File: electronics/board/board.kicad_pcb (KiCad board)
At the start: 2 copper layers, 58 parts, among them J1 Screw_Terminal_01x02, J10 Conn_01x02, J11 Conn_01x02, J12 Conn_01x02, J13 Conn_01x02, J14 Conn_01x02, J15 Conn_01x02, J16 Conn_01x02, J17 Conn_01x02, J18 Conn_01x02, J19 Conn_01x02, J2 Screw_Terminal_01x02, J20 Conn_01x02, J21 Conn_01x02, J22 Conn_01x02, J23 Screw_Terminal_01x01, J25 Screw_Terminal_01x01, J3 AVR-ISP-6, J4 USB_B_Micro, J5 Screw_Terminal_01x02, J6 Screw_Terminal_01x02, J7 Conn_01x02, J8 Conn_01x02, J9 Conn_01x02, Q1 IRF7404, SW1 SW_Push_Open_Dual, U1 LMV358, U2 ATmega32U4-AU, U3 LM7805_TO220, U4 ST485EBDR, U5 ULN2803A, U6 ULN2803A, Y1 Crystal 16MHz

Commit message: Footprint placement v1
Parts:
- moved J5 152.0 mm to (182.9, 147.3), turned to 180 degrees
- moved D3 143.0 mm to (202.9, 163.8)
- moved D2 142.6 mm to (174.0, 147.2)
- moved C7 136.8 mm to (181.1, 161.3), turned to 0 degrees
- moved R3 136.7 mm to (187.5, 161.3)
- moved R7 136.4 mm to (198.6, 163.8)
- moved U3 132.9 mm to (168.9, 146.1), turned to 180 degrees
- moved D1 130.3 mm to (189.7, 153.7)
- moved SW1 129.4 mm to (191.1, 146.7)
- moved U4 126.4 mm to (156.4, 147.3), turned to 180 degrees
- moved R8 122.9 mm to (159.5, 152.4), turned to 0 degrees
- moved J6 112.7 mm to (199.4, 148.6)
- moved J1 101.8 mm to (71.1, 146.1)
- moved J2 94.5 mm to (69.8, 160.0)
- moved J4 90.1 mm to (203.3, 157.1)
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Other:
- board outline added: 141 x 30.5 mm

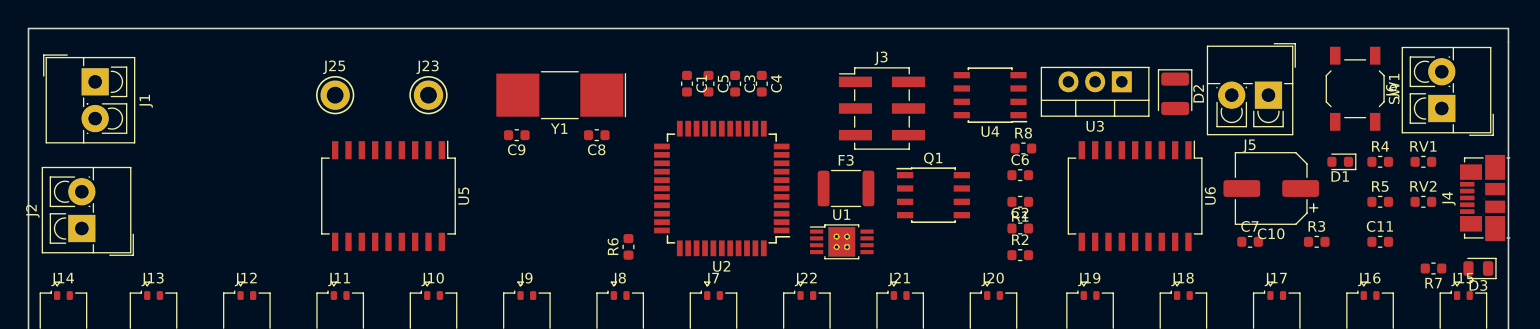
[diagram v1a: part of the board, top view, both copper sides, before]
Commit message: 5V regulator bug
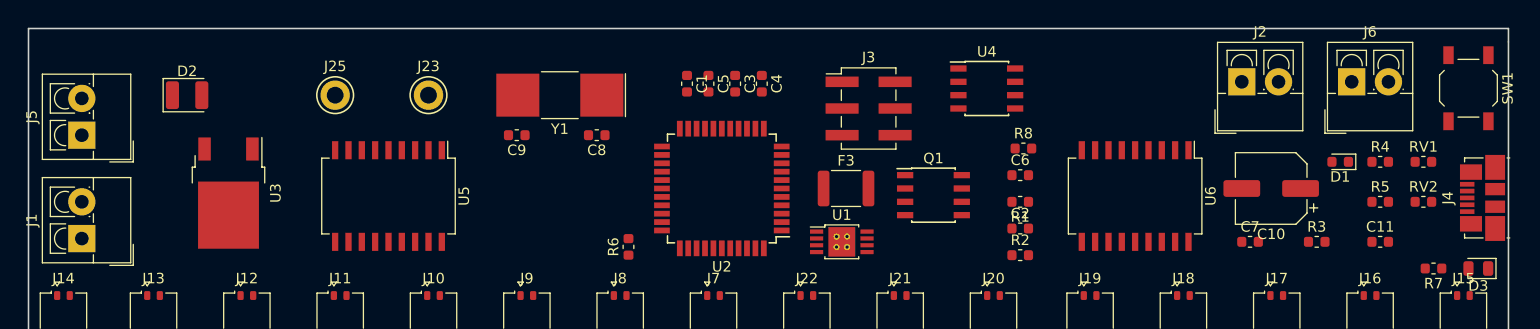
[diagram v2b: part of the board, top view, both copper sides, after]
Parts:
- U3: value LM7805_TO220 -> NCP1117-5.0_TO252; footprint Package_TO_SOT_THT:TO-220-3_Vertical -> Package_TO_SOT_SMD:TO-252-2
- moved J5 113.1 mm to (69.8, 151.1), turned to 90 degrees
- moved J2 111.4 mm to (180.3, 146.1), turned to 0 degrees
- moved D2 94.1 mm to (79.9, 147.3), turned to 0 degrees
- moved U3 85.7 mm to (83.8, 156.7), turned to 270 degrees
- moved J1 15.0 mm to (69.8, 161.0), turned to 90 degrees
- moved SW1 10.8 mm to (201.9, 146.7)
- moved J6 8.95 mm to (190.8, 146.1), turned to 0 degrees
- moved J3 1.27 mm to (144.8, 148.6)
- moved U4 0.71 mm to (156.1, 146.7), turned to 0 degrees
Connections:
- U3 pad 1: +12V -> GND
- U3 pad 2: GND -> +5V
- U3 pad 3: +5V -> +12V

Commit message: Routing update
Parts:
- moved C9 25.6 mm to (136.4, 146.1)
- moved C1 22.6 mm to (110.8, 161.4)
- moved C5 21.5 mm to (114.3, 161.4)
- moved C3 20.8 mm to (117.9, 161.4)
- moved C4 20.1 mm to (121.5, 161.4)
- moved J25 14.7 mm to (108.5, 144.5)
- moved C8 13.6 mm to (131.5, 146.1)
- moved J23 10.3 mm to (112.8, 144.5)
- moved R6 7.64 mm to (121.4, 154.2), turned to 270 degrees
- moved R1 7.46 mm to (153.2, 161.8), turned to 270 degrees
- moved Y1 6.43 mm to (121.5, 145.3), turned to 0 degrees
- moved R5 5.43 mm to (192.5, 162.8)
- moved C11 2.50 mm to (192.5, 159.0)
- moved Q1 1.89 mm to (152.6, 155.8)
- moved R7 1.79 mm to (197.1, 162.8)
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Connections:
- J1 pad 1: +12V -> Net-(D2-Pad1)
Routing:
- net +5V: track 0.00 -> 226.6 mm, vias 0 -> 3
- net /RESET: track 0.00 -> 95.4 mm, vias 0 -> 3
- net +12V: track 0.00 -> 92.4 mm, vias 0 -> 2
- net Net-(J10-Pad2): track 0.00 -> 80.8 mm, vias 0 -> 2
- net Net-(J15-Pad2): track 0.00 -> 80.6 mm, vias 0 -> 2
- net Net-(F3-Pad2): track 0.00 -> 67.8 mm, vias 0 -> 2
- net VBUS: track 0.00 -> 66.5 mm, vias 0 -> 3
- net Net-(R4-Pad1): track 0.00 -> 65.5 mm, vias 0 -> 4
- net Net-(R5-Pad1): track 0.00 -> 57.4 mm, vias 0 -> 2
- net Net-(U2-Pad26): track 0.00 -> 54.3 mm, vias 0 -> 2
- net Net-(U2-Pad27): track 0.00 -> 52.0 mm, vias 0 -> 2
- net Net-(U2-Pad41): track 0.00 -> 45.2 mm, vias 0 -> 2
- net Net-(U2-Pad40): track 0.00 -> 44.9 mm, vias 0 -> 2
- net Net-(U2-Pad39): track 0.00 -> 44.5 mm, vias 0 -> 2
- net Net-(U2-Pad37): track 0.00 -> 44.4 mm, vias 0 -> 2
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
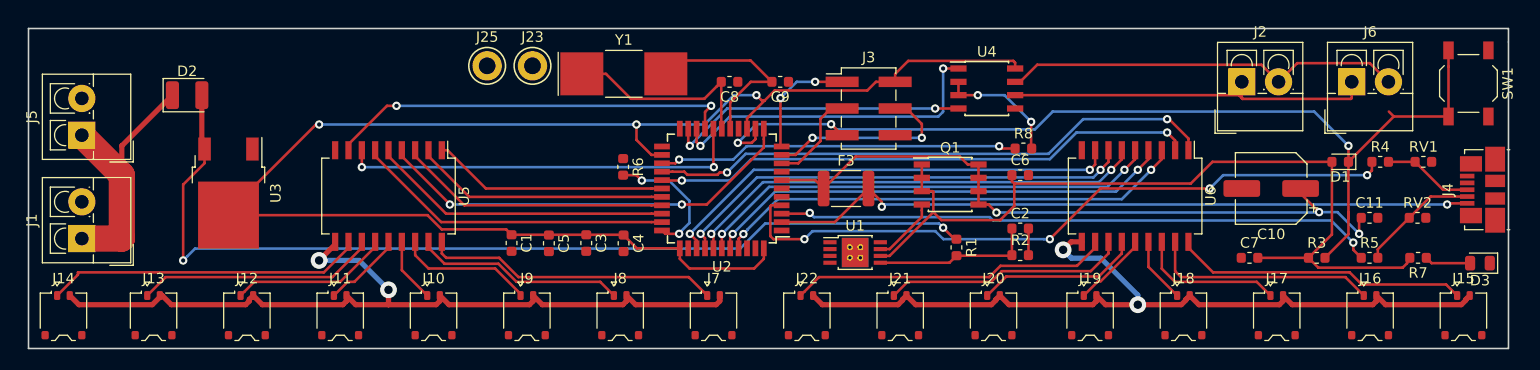
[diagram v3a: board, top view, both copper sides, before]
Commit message: GND + mounting holes
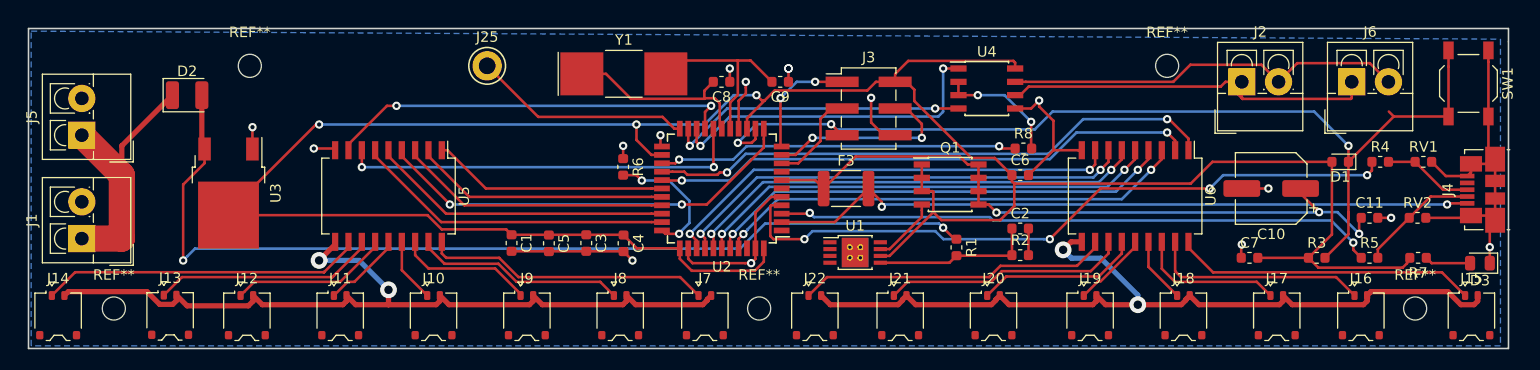
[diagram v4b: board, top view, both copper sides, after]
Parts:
- removed J23: Screw_Terminal_01x01, TestPoint:TestPoint_Keystone_5005-5009_Compact
- added REF**: MountingHole_2.2mm_M2, MountingHole:MountingHole_2.2mm_M2, F.Cu at (134.4, 167.6)
- added REF**: MountingHole_2.2mm_M2, MountingHole:MountingHole_2.2mm_M2, F.Cu at (196.8, 167.6)
- added REF**: MountingHole_2.2mm_M2, MountingHole:MountingHole_2.2mm_M2, F.Cu at (72.9, 167.6)
- added REF**: MountingHole_2.2mm_M2, MountingHole:MountingHole_2.2mm_M2, F.Cu at (173.2, 144.5)
- added REF**: MountingHole_2.2mm_M2, MountingHole:MountingHole_2.2mm_M2, F.Cu at (85.9, 144.5)
- moved J13 1.58 mm to (78.3, 168.2)
- moved J16 0.88 mm to (191.7, 168.3)
- moved J7 0.83 mm to (129.2, 168.3)
- moved C8 0.76 mm to (130.8, 146.1)
- moved J15 0.76 mm to (202.2, 168.3)
- moved J22 0.76 mm to (139.7, 168.3)
- moved J14 0.51 mm to (67.6, 168.3)
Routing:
- net GND: track 0.00 -> 100.9 mm, vias 0 -> 17
- net Net-(J25-Pad1): track 0.00 -> 20.8 mm
- net +5V: track 226.6 -> 242.4 mm
- net Net-(J13-Pad1): track 22.9 -> 21.7 mm
- net Net-(J16-Pad1): track 21.7 -> 20.8 mm
- net Net-(J7-Pad1): track 28.1 -> 27.2 mm
- net Net-(J2-Pad1): track 35.4 -> 36.3 mm
- net Net-(J22-Pad1): track 30.5 -> 29.7 mm
- net Net-(J15-Pad1): track 28.0 -> 28.8 mm
- net Net-(J15-Pad2): track 80.6 -> 81.2 mm
- net Net-(C8-Pad2): track 19.4 -> 18.9 mm
- added copper zone on B.Cu, net GND

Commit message: Edited Silks layers
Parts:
- moved REF** 1.78 mm to (84.1, 144.5)
- moved D2 0.76 mm to (79.9, 148.1)
- renumbered J25 to PD5
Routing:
- net /RESET: track 95.4 -> 94.8 mm
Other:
- board text added: "- +"
- board text added: "12VDC"
- board text added: "A+ B-"
- board text added: "AVR ISP↓"
- board text added: "B- A+"
- board text added: "PWR LED"
- board text added: "Paraf Yún PCB 1.0"
- board text added: "Paraf Yún PCB 1.0 Yoan Mollard"
- board text added: "RESET"
- board text added: "RS485"
- board text added: "RS485→"

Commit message: Silk update
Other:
- board text added: "1:MISO 2:5V 3:SCK 4:MOSI"
- board text added: "AVR ISP↘"
- board text removed: "AVR ISP↓"
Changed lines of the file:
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@@
   (general
     (thickness 1.6)
-    (drawings 22)
+    (drawings 23)
     (tracks 668)
     (zones 0)
@@
     (tags "Surface mounted pin header SMD 2x03 2.54mm double row")
     (attr smd)
-    (fp_text reference J3 (at 4.303 -5.588) (layer F.SilkS)
+    (fp_text reference J3 (at 6.081 -5.588) (layer F.SilkS)
       (effects (font (size 1 1) (thickness 0.15)))
     )
@@
     (tags "SPST Tactile Switch")
     (attr smd)
-    (fp_text reference SW1 (at 0 -3.75 270) (layer F.SilkS)
+    (fp_text reference SW1 (at -3.708 0) (layer F.SilkS)
       (effects (font (size 1 1) (thickness 0.15)))
     )
@@
     (pad 1 np_thru_hole circle (at 0 0) (size 2.2 2.2) (drill 2.2) (layers *.Cu *.Mask))
   )
+  (gr_text "1:MISO  2:5V\n3:SCK   4:MOSI" (at 140.208 143.002) (layer F.SilkS)
+    (effects (font (size 0.75 0.75) (thickness 0.1875)) (justify left))
+  )
   (gr_text "-\n\n+" (at 76.454 159.004) (layer B.SilkS)
     (effects (font (size 1.5 1.5) (thickness 0.3)))
@@
     (effects (font (size 1.5 1.5) (thickness 0.3)))
   )
-  (gr_text "AVR ISP↓" (at 140.462 143.002) (layer F.SilkS)
+  (gr_text "AVR ISP↘" (at 133.858 143.002) (layer F.SilkS)
     (effects (font (size 1.5 1.5) (thickness 0.3)))
   )

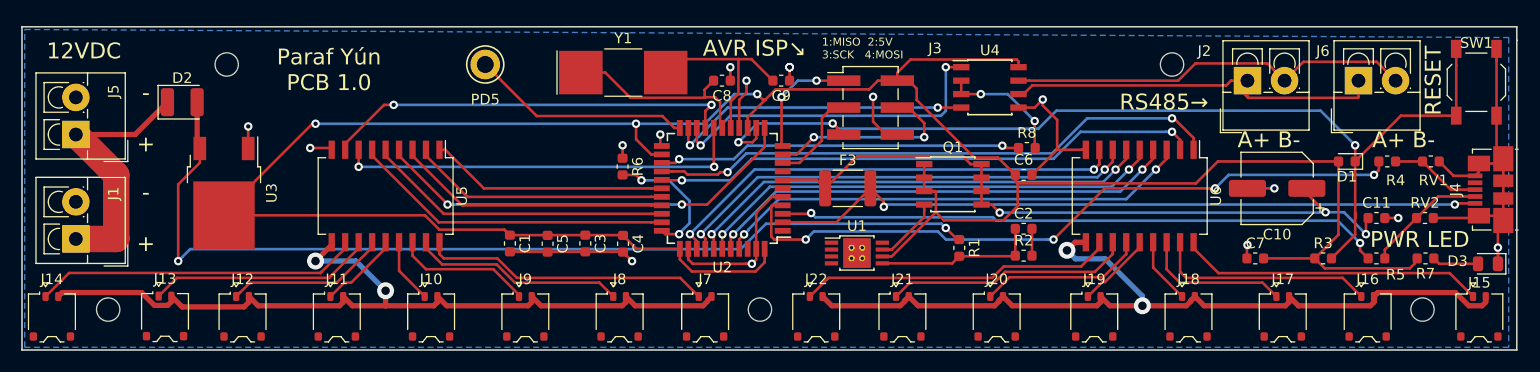
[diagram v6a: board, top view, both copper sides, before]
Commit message: Final routing and copper zones
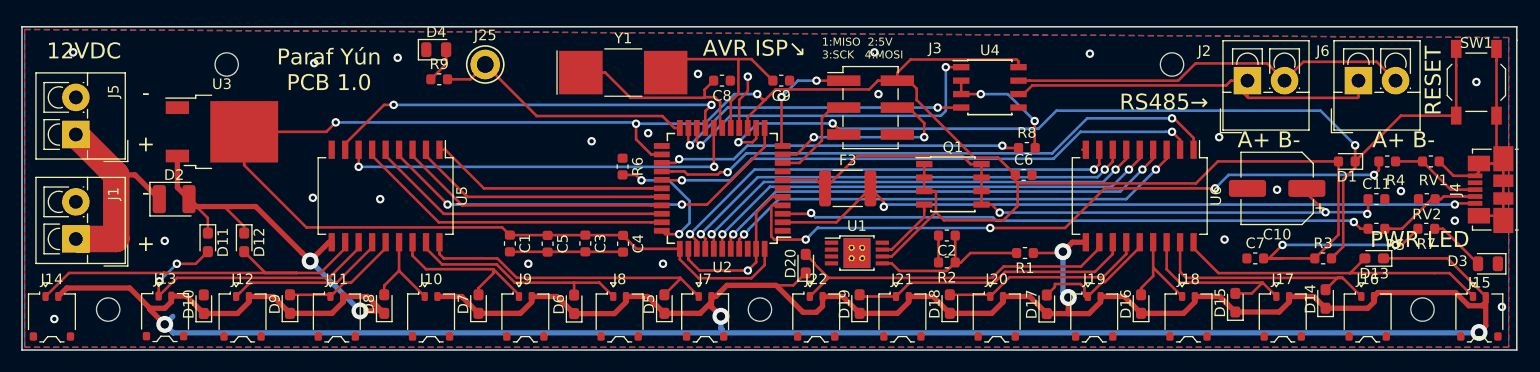
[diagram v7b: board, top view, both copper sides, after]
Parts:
- removed PD5: Screw_Terminal_01x01, TestPoint:TestPoint_Keystone_5005-5009_Compact
- added D10: D, Diode_SMD:D_0603_1608Metric_Pad1.05x0.95mm_HandSolder, F.Cu at (81.9, 167.1)
- added D11: D, Diode_SMD:D_0603_1608Metric_Pad1.05x0.95mm_HandSolder, F.Cu at (82.3, 161.3)
- added D12: D, Diode_SMD:D_0603_1608Metric_Pad1.05x0.95mm_HandSolder, F.Cu at (85.7, 161.3)
- added D13: D, Diode_SMD:D_0603_1608Metric_Pad1.05x0.95mm_HandSolder, F.Cu at (192.3, 162.8)
- added D14: D, Diode_SMD:D_0603_1608Metric_Pad1.05x0.95mm_HandSolder, F.Cu at (187.7, 166.6)
- added D15: D, Diode_SMD:D_0603_1608Metric_Pad1.05x0.95mm_HandSolder, F.Cu at (179.2, 167.0)
- added D16: D, Diode_SMD:D_0603_1608Metric_Pad1.05x0.95mm_HandSolder, F.Cu at (170.3, 167.1)
- added D17: D, Diode_SMD:D_0603_1608Metric_Pad1.05x0.95mm_HandSolder, F.Cu at (161.4, 167.1)
- added D18: D, Diode_SMD:D_0603_1608Metric_Pad1.05x0.95mm_HandSolder, F.Cu at (152.3, 167.1)
- added D19: D, Diode_SMD:D_0603_1608Metric_Pad1.05x0.95mm_HandSolder, F.Cu at (143.8, 167.1)
- added D20: D, Diode_SMD:D_0603_1608Metric_Pad1.05x0.95mm_HandSolder, F.Cu at (138.7, 163.3)
- added D4: LED, LED_SMD:LED_0805_2012Metric, F.Cu at (103.8, 143.1)
- added D5: D, Diode_SMD:D_0603_1608Metric_Pad1.05x0.95mm_HandSolder, F.Cu at (125.3, 167.1)
- added D6: D, Diode_SMD:D_0603_1608Metric_Pad1.05x0.95mm_HandSolder, F.Cu at (116.8, 167.1)
- added D7: D, Diode_SMD:D_0603_1608Metric_Pad1.05x0.95mm_HandSolder, F.Cu at (107.8, 167.1)
- added D8: D, Diode_SMD:D_0603_1608Metric_Pad1.05x0.95mm_HandSolder, F.Cu at (98.9, 167.1)
- added D9: D, Diode_SMD:D_0603_1608Metric_Pad1.05x0.95mm_HandSolder, F.Cu at (90.0, 167.1)
- added J25: Screw_Terminal_01x01, TestPoint:TestPoint_Keystone_5005-5009_Compact, F.Cu at (108.5, 144.5)
- added R9: 1k, Resistor_SMD:R_0603_1608Metric, F.Cu at (104.1, 145.9)
- moved D2 9.18 mm to (79.1, 157.2)
- moved C2 7.27 mm to (152.0, 160.7), turned to 180 degrees
- moved R2 7.27 mm to (152.0, 163.2), turned to 180 degrees
- moved R1 6.22 mm to (159.4, 162.3), turned to 180 degrees
- moved U3 5.78 mm to (83.6, 150.9), turned to 0 degrees
- moved R7 2.80 mm to (197.2, 160.0)
- moved R5 2.79 mm to (192.5, 160.0)
- moved RV2 1.79 mm to (197.3, 157.2), turned to 180 degrees
- moved C11 1.78 mm to (192.5, 157.2)
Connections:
- J10 pad 2: Net-(J10-Pad2) -> +12V
- J11 pad 2: Net-(J10-Pad2) -> +12V
- J12 pad 2: Net-(J10-Pad2) -> +12V
- J13 pad 2: Net-(J10-Pad2) -> +12V
- J14 pad 2: Net-(J10-Pad2) -> +12V
- J15 pad 2: Net-(J15-Pad2) -> +12V
- J16 pad 2: Net-(J15-Pad2) -> +12V
- J17 pad 2: Net-(J15-Pad2) -> +12V
- J18 pad 2: Net-(J15-Pad2) -> +12V
- J19 pad 2: Net-(J15-Pad2) -> +12V
- J20 pad 2: Net-(J15-Pad2) -> +12V
- J21 pad 2: Net-(J15-Pad2) -> +12V
- J22 pad 2: Net-(J15-Pad2) -> +12V
- J7 pad 2: Net-(J10-Pad2) -> +12V
- J8 pad 2: Net-(J10-Pad2) -> +12V
- J9 pad 2: Net-(J10-Pad2) -> +12V
- U5 pad 10: Net-(J10-Pad2) -> +12V
- U6 pad 10: Net-(J15-Pad2) -> +12V
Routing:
- net +12V: track 92.0 -> 354.3 mm, vias 2 -> 7
- net Net-(J15-Pad2): track 81.2 -> 0.00 mm, vias 2 -> 0
- net Net-(J10-Pad2): track 81.1 -> 0.00 mm, vias 2 -> 0
- net GND: track 100.9 -> 60.0 mm, vias 17 -> 24
- net Net-(D11-Pad2): track 21.7 -> 28.9 mm, vias 0 -> 2
- net Net-(D12-Pad2): track 30.8 -> 36.8 mm
- net +5V: track 242.4 -> 248.0 mm, vias 3 -> 5
- net Net-(D17-Pad2): track 7.29 -> 12.7 mm
- net Net-(D2-Pad1): track 25.1 -> 20.2 mm
- net Net-(J25-Pad1): track 20.8 -> 25.0 mm
- net Net-(D18-Pad2): track 15.6 -> 19.5 mm
- net Net-(D9-Pad2): track 7.65 -> 11.5 mm
- net Net-(D19-Pad2): track 23.2 -> 26.7 mm
- net Net-(D4-Pad2): track 0.00 -> 3.39 mm
- net Net-(D20-Pad2): track 29.7 -> 32.9 mm
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- added copper zone on F.Cu, net GND

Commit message: Switching to 0805
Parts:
- C1, C11, C2, C3, C4, C5, C6, C7, C8, C9: footprint Capacitor_SMD:C_0603_1608Metric -> Capacitor_SMD:C_0805_2012Metric_Pad1.15x1.40mm_HandSolder
- D1: footprint Diode_SMD:D_0603_1608Metric -> Diode_SMD:D_0805_2012Metric_Pad1.15x1.40mm_HandSolder
- D10, D11, D12, D13, D14, D15, D16, D17, D18, D19, D20, D5, D6, D7, D8, D9: footprint Diode_SMD:D_0603_1608Metric_Pad1.05x0.95mm_HandSolder -> Diode_SMD:D_0805_2012Metric_Pad1.15x1.40mm_HandSolder
- R1, R2, R3, R4, R5, R6, R7, R8, R9, RV1, RV2: footprint Resistor_SMD:R_0603_1608Metric -> Resistor_SMD:R_0805_2012Metric_Pad1.15x1.40mm_HandSolder
- moved D4 1.07 mm to (104.0, 144.2)
- moved R9 1.03 mm to (104.0, 146.9)
- moved C8 0.94 mm to (129.9, 145.9), turned to 270 degrees
- moved C1 0.86 mm to (111.6, 161.4)
- moved D1 0.44 mm to (189.3, 153.7)
- moved C5 0.41 mm to (114.8, 161.4)
- moved R2 0.25 mm to (152.0, 162.9)
- moved R4 0.07 mm to (193.5, 153.7)
- moved C3 0.05 mm to (117.9, 161.4)
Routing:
- net GND: track 60.0 -> 49.4 mm, vias 24 -> 22
- net +5V: track 248.0 -> 253.7 mm, vias 5 -> 7
- net Net-(D10-Pad2): track 15.2 -> 18.4 mm
- net /MISO: track 11.2 -> 12.5 mm
- net Net-(C8-Pad2): track 18.9 -> 18.1 mm
- net Net-(J4-Pad2): track 9.78 -> 10.3 mm
